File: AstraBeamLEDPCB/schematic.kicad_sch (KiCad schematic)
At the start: 9 parts, among them J1 Conn_01x01_Pin, J2 Conn_01x01_Pin, J3 Conn_01x01_Pin, J4 Conn_01x01_Pin, J5 Conn_01x01_Pin, J6 Conn_01x01_Pin, J7 Conn_01x01_Pin, J8 Conn_01x01_Pin, U1 LERTDCYS2WN

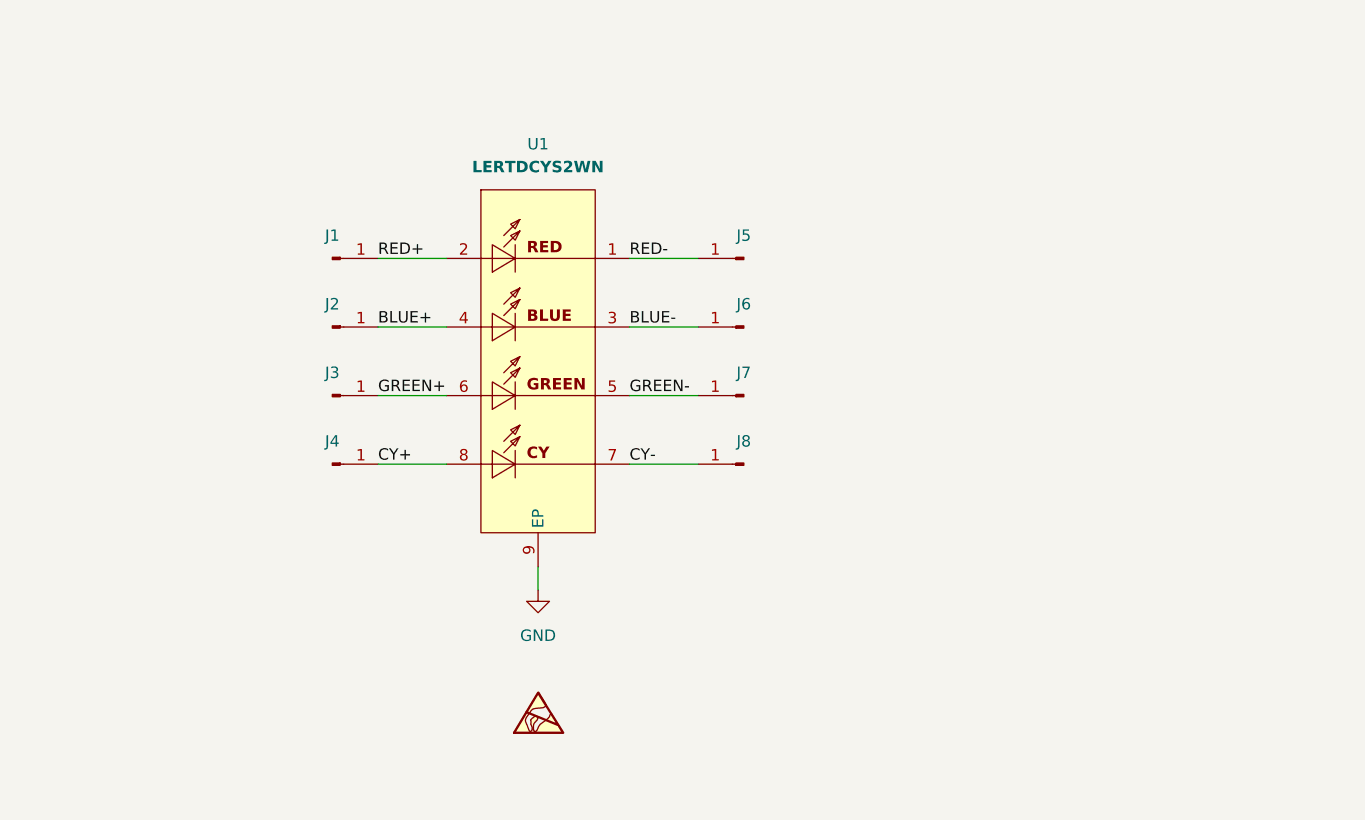
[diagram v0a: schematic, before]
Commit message: Added ti connectors
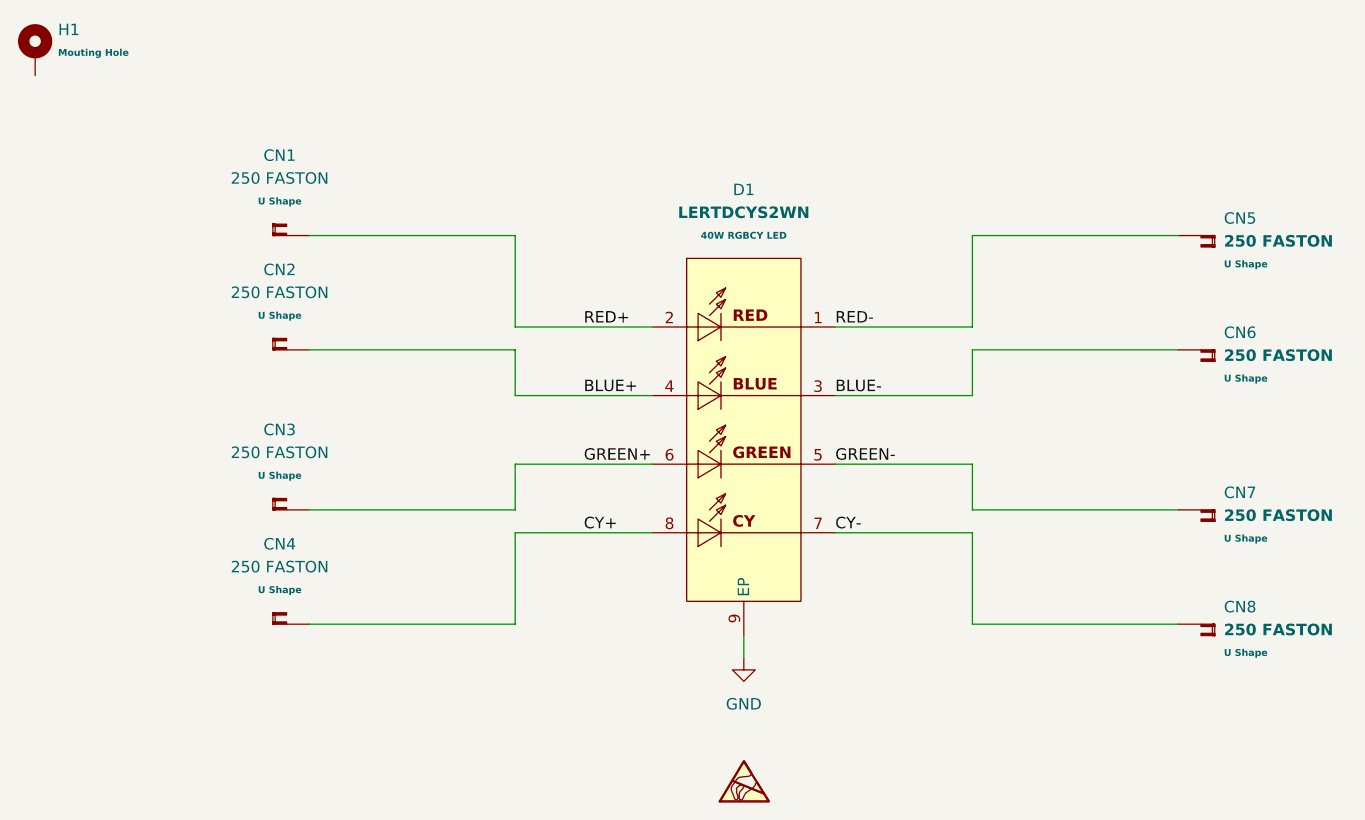
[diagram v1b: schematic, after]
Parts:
- removed J1, J2, J3, J4, J5, J6, J7, J8: Conn_01x01_Pin, Connector_Wire:SolderWirePad_1x01_SMD_5x10mm, symbol Connector:Conn_01x01_Pin
- removed U1: LERTDCYS2WN, EASYEDA2KICAD:LED_LERTDCYS2WN, symbol EASYEDA2KICAD:LED_RGBA_3A_LERTDCYS2WN
- added CN1, CN2, CN3, CN4, CN5, CN6, CN7, CN8: 250 FASTON, LiveAstra:CN_FASTON_250__41290_U, symbol LiveAstra:CN_FASTON_250__41290_U
- added D1: LERTDCYS2WN, LiveAstra:LED_LERTDCYS2WN, symbol LiveAstra:LED_RGBA_3A_LERTDCYS2WN
- added H1: MountingHole_Pad, MountingHole:MountingHole_5.3mm_M5_DIN965_Pad, symbol LiveAstra:MountingHole_Pad
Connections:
- net BLUE+: now also CN2.1, D1.4
- net BLUE-: now also CN6.1, D1.3
- net CY+: now also CN4.1, D1.8
- net CY-: now also CN8.1, D1.7
- net GND: now also D1.9 (EP)
- net GREEN+: now also CN3.1, D1.6
- net GREEN-: now also CN7.1, D1.5
- net RED+: now also CN1.1, D1.2
- net RED-: now also CN5.1, D1.1

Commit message: Redesigned pcb for smaller size
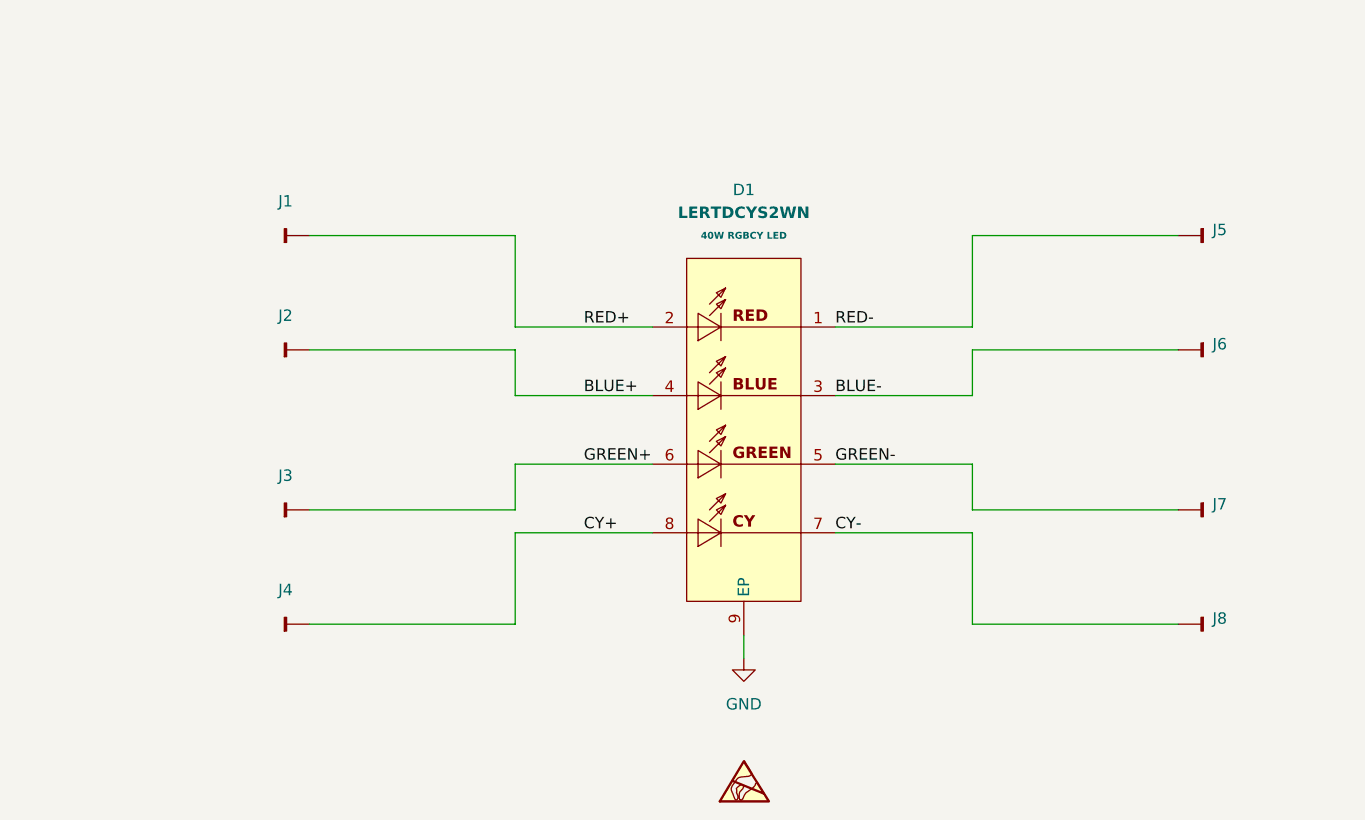
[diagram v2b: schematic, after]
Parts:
- removed CN1, CN2, CN3, CN4, CN5, CN6, CN7, CN8: 250 FASTON, LiveAstra:CN_FASTON_250__41290_U, symbol LiveAstra:CN_FASTON_250__41290_U
- removed H1: MountingHole_Pad, MountingHole:MountingHole_5.3mm_M5_DIN965_Pad, symbol LiveAstra:MountingHole_Pad
- added J1, J2, J3, J4, J5, J6, J7, J8: ~, LiveAstra:SolderWirePad_1x01_SMD_5x10mm, symbol LiveAstra:J_1_SolderPad
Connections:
- net BLUE+: now also J2.1
- net BLUE-: now also J6.1
- net CY+: now also J4.1
- net CY-: now also J8.1
- net GREEN+: now also J3.1
- net GREEN-: now also J7.1
- net RED+: now also J1.1
- net RED-: now also J5.1
